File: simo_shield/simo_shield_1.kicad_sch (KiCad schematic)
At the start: 11 parts, among them J1 Conn_01x02_Female, J2 Conn_01x02_Female, J3 Conn_01x01_Female, U1 elemon_board, U2 modulo_flash_externa, U3 bluepill_board_stm32, U4 modulo_acelerometro

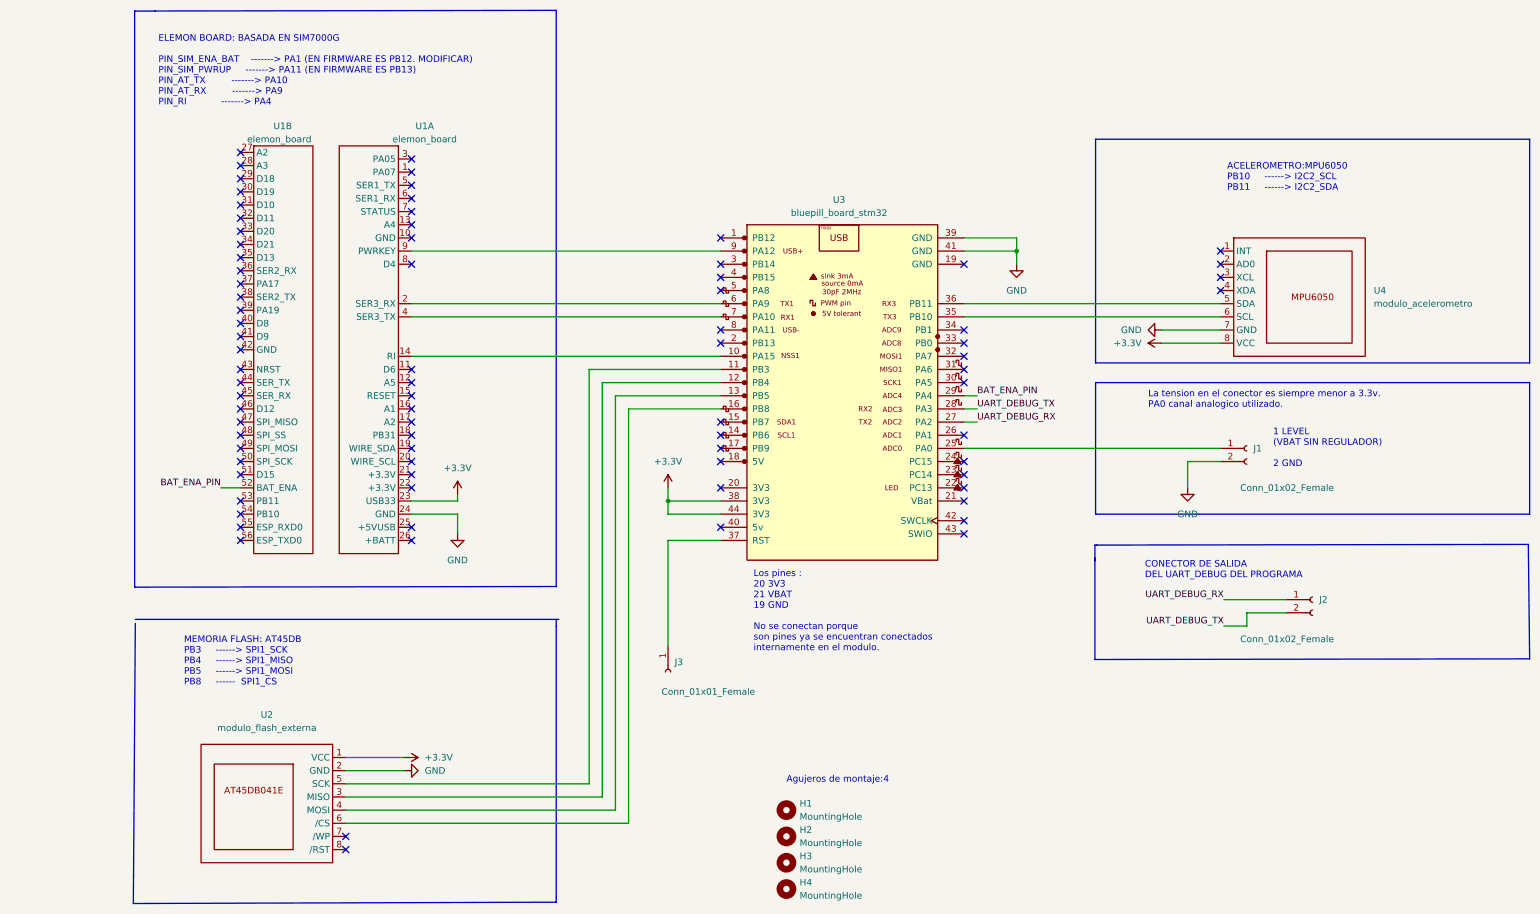
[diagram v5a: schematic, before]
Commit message: modificaciones miniimas  a esquematico para mejorar prolijidad
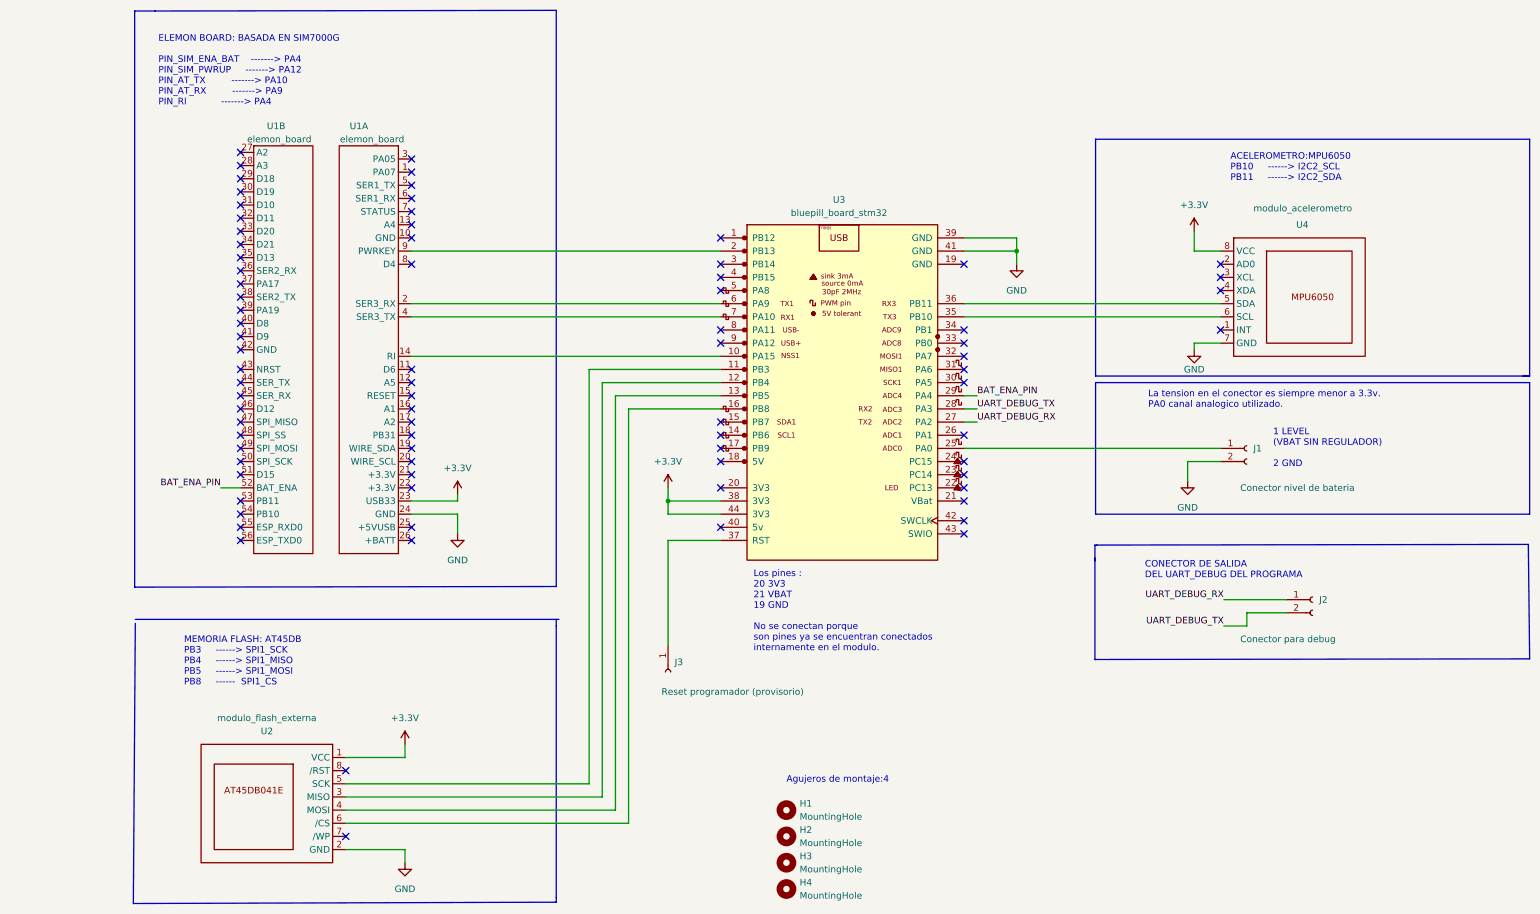
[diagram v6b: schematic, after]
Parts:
- J1: value Conn_01x02_Female -> Conector nivel de bateria
- J2: value Conn_01x02_Female -> Conector para debug
- J3: value Conn_01x01_Female -> Reset programador (provisorio)
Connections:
- net at U1.9 (PWRKEY): now also U3.2 (PB13); no longer U3.9 (PA12)
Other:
- note added: "ELEMON BOARD: BASADA EN SIM7000G PIN_SIM_ENA_BAT -------> PA4 PIN_SIM_PWRUP -------> PA12 PIN_AT_TX -------> PA10 PIN_AT_RX -------> PA9 PIN_RI -------> PA4"
- note removed: "ELEMON BOARD: BASADA EN SIM7000G PIN_SIM_ENA_BAT -------> PA1 (EN FIRMWARE ES PB12. MODIFICAR) PIN_SIM_PWRUP -------> PA11 (EN FIRMWARE ES PB13) PIN_AT_TX -------> PA10 PIN_AT_RX -------> PA9 PIN_RI -------> PA4"

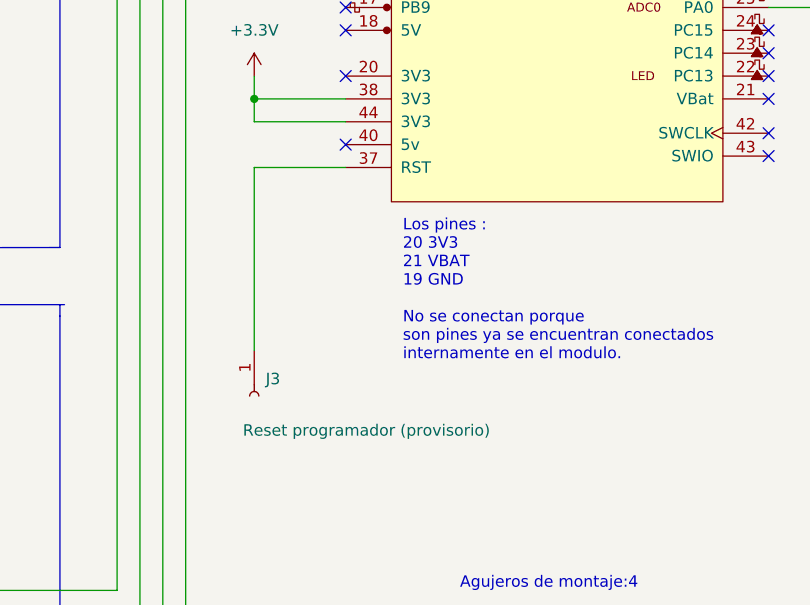
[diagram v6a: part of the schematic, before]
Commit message: [simo shield] Se elimino plano de tierra
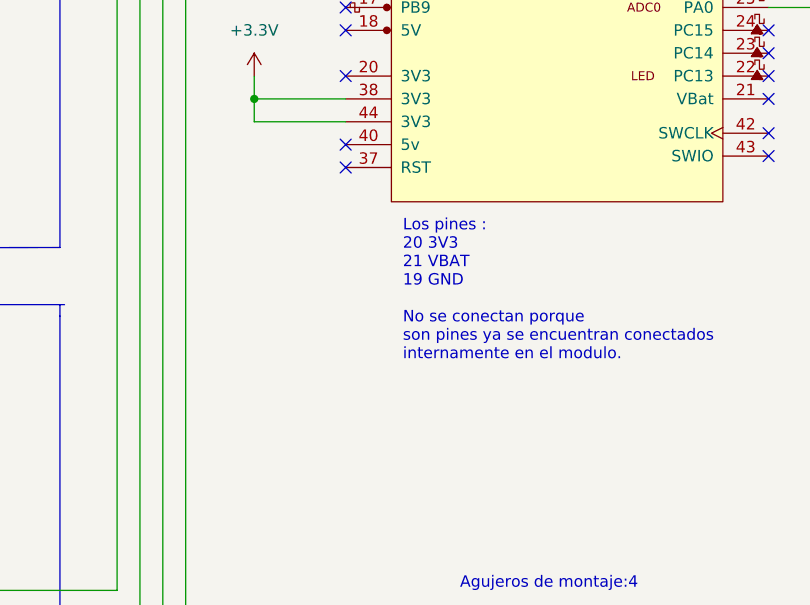
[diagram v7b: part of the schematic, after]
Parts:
- removed J3: Reset programador (provisorio), Connector_PinHeader_2.54mm:PinHeader_1x01_P2.54mm_Vertical, symbol simo_shield:Conn_01x01_Female
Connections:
- no-connect marks 80 -> 81
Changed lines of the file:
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@@
   (junction (at 184.15 62.23) (diameter 0) (color 0 0 0 0)
   )
+  (no_connect (at 127 118.11))
   (no_connect (at 127 77.47))
   (no_connect (at 127 69.85))
@@
     (stroke (width 0) (type default) (color 0 0 0 0))
   )
-  (wire (pts (xy 127 118.11) (xy 116.84 118.11))
-    (stroke (width 0) (type default) (color 0 0 0 0))
-  )
   (wire (pts (xy 173.99 92.71) (xy 176.53 92.71))
     (stroke (width 0) (type default) (color 0 0 0 0))
@@
   )
   (wire (pts (xy 116.84 107.95) (xy 116.84 110.49))
-    (stroke (width 0) (type default) (color 0 0 0 0))
-  )
-  (wire (pts (xy 116.84 118.11) (xy 116.84 138.43))
     (stroke (width 0) (type default) (color 0 0 0 0))
   )
@@
     (pin "7")
     (pin "8")
-  )
-  (symbol (lib_id "simo_shield:Conn_01x01_Female") (at 116.84 143.51 270) (unit 1)
-    (in_bom yes) (on_board yes)
-    (property "Reference" "J3" (id 0) (at 118.11 141.6049 90)
-      (effects (font (size 1.27 1.27)) (justify left))
-    )
-    (property "Value" "Reset programador (provisorio)" (id 1) (at 115.57 147.32 90)
-      (effects (font (size 1.27 1.27)) (justify left))
-    )
-    (property "Footprint" "Connector_PinHeader_2.54mm:PinHeader_1x01_P2.54mm_Vertical" (id 2) (at 116.84 143.51 0)
-      (effects (font (size 1.27 1.27)) hide)
-    )
-    (property "Datasheet" "~" (id 3) (at 116.84 143.51 0)
-      (effects (font (size 1.27 1.27)) hide)
-    )
-    (pin "1")
   )
   (symbol (lib_name "elemon_board_1") (lib_id "simo_shield:elemon_board") (at 64.77 40.64 0) (mirror y) (unit 1)
@@
       (reference "J2") (unit 1) (value "Conector para debug") (footprint "simo_shield:JST_EH_B2B-EH-A_1x02_P2.50mm_Vertical")
     )
-    (path "/59284322-711a-4de1-98eb-cc82830fd394"
-      (reference "J3") (unit 1) (value "Reset programador (provisorio)") (footprint "Connector_PinHeader_2.54mm:PinHeader_1x01_P2.54mm_Vertical")
-    )
     (path "/5da0ae67-8451-47ba-8f38-5b0fec97941b"
